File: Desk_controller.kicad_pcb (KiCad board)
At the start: 2 copper layers, 100 x 51.2 mm, 105 parts, among them J1 B4B XH A, J2 01x04 socket, J3 01x14 socket, J4 HX JN1.27-2x5 WZ H4.9, J5 USB_C_Receptacle_USB2.0_16P, J6 Dell DC jack, J7 B6B XH A, J8 DC barrel assy, U1 LMR38020, U2 STM32G431K8T, U3 VNH7070, U4 USBLC6-2SC6, Y1 20 MHz

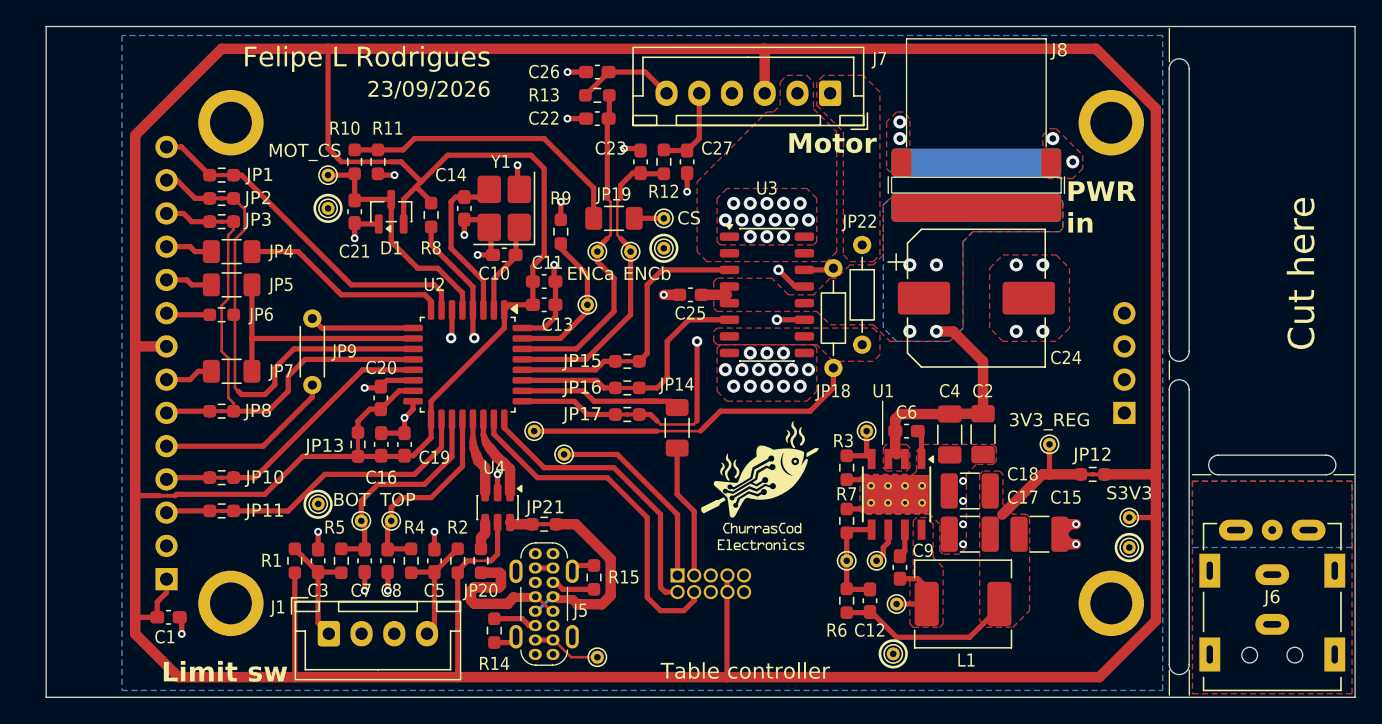
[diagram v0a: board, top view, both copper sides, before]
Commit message: Make project libraries and 3D models self-contained
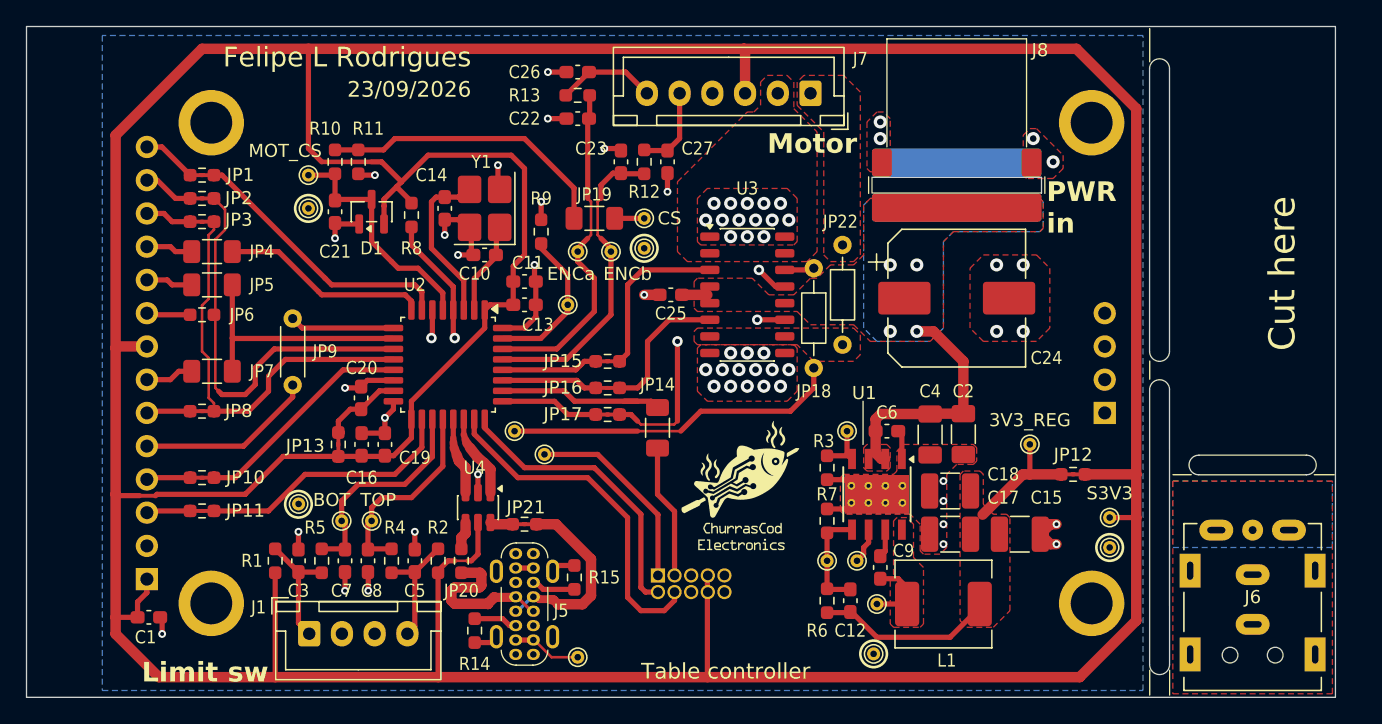
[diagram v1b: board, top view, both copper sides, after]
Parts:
- U1: value LMR38020 -> LMR380x0; footprint Package_SO:Texas_HSOP-8-1EP_3.9x4.9mm_P1.27mm_ThermalVias -> Personal:Texas_HSOP-8-1EP_3.9x4.9mm_P1.27mm_ThermalVias_w_step
- moved R8 1.50 mm to (127.9, 54.4)
- moved C1 1.50 mm to (107.8, 85.1)
- moved C10 1.50 mm to (133.5, 57.5)
- moved C11 1.50 mm to (136.5, 59.5)
- moved C12 1.50 mm to (161.4, 83.9)
- moved C13 1.50 mm to (136.5, 61.3)
- moved C14 1.50 mm to (130.5, 53.9)
- moved C15 1.50 mm to (174.4, 78.8)
- moved C16 1.50 mm to (124.1, 71.9)
- moved C17 1.50 mm to (169.1, 78.8)
- moved C18 1.50 mm to (169.1, 75.5)
- moved C19 1.50 mm to (125.9, 71.9)
- moved C2 1.50 mm to (170.1, 71.1)
- moved C20 1.50 mm to (124.1, 68.4)
- moved C21 1.50 mm to (122.1, 54.1)
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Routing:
- net /System overview/Block diagram/S19V5: track 20.0 -> 20.8 mm
- removed copper zone on F.Cu, net (none)
